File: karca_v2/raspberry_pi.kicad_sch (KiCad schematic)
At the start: 10 parts, among them J12 Conn_02x10_Odd_Even, Q2 PN2222A, U13 M41T93

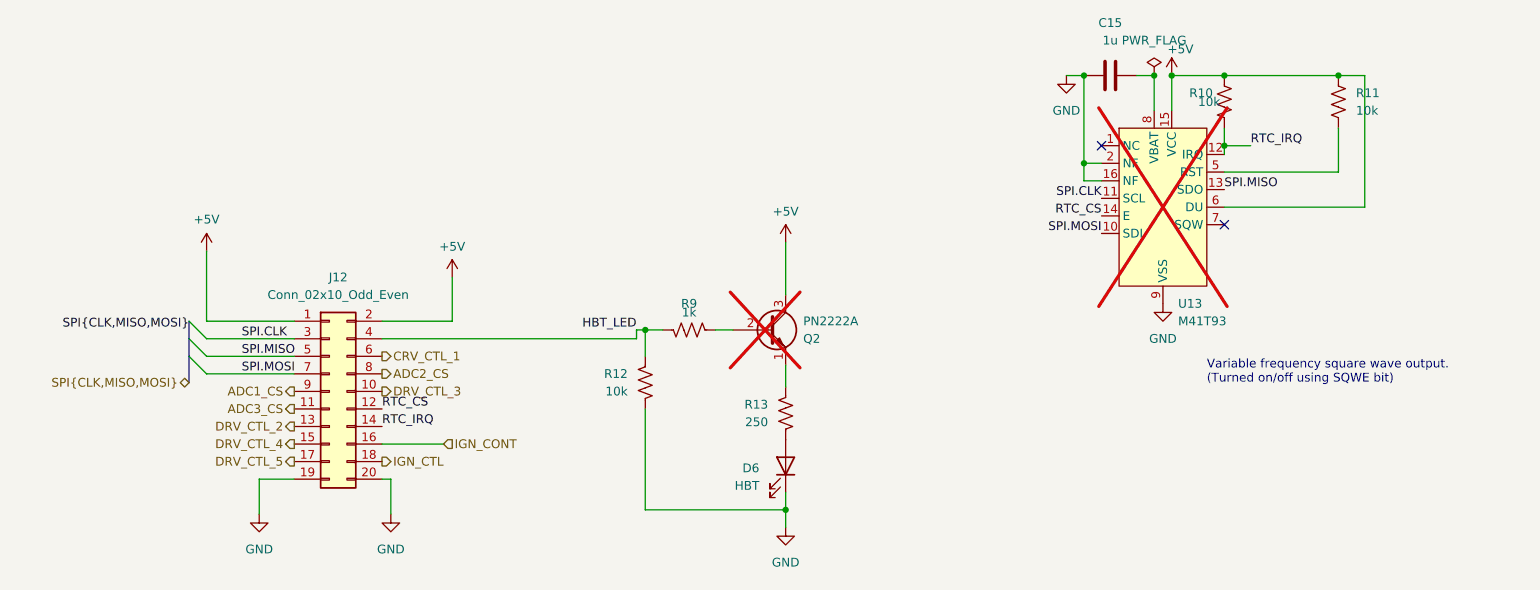
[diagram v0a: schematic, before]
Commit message: reorganized ADCs
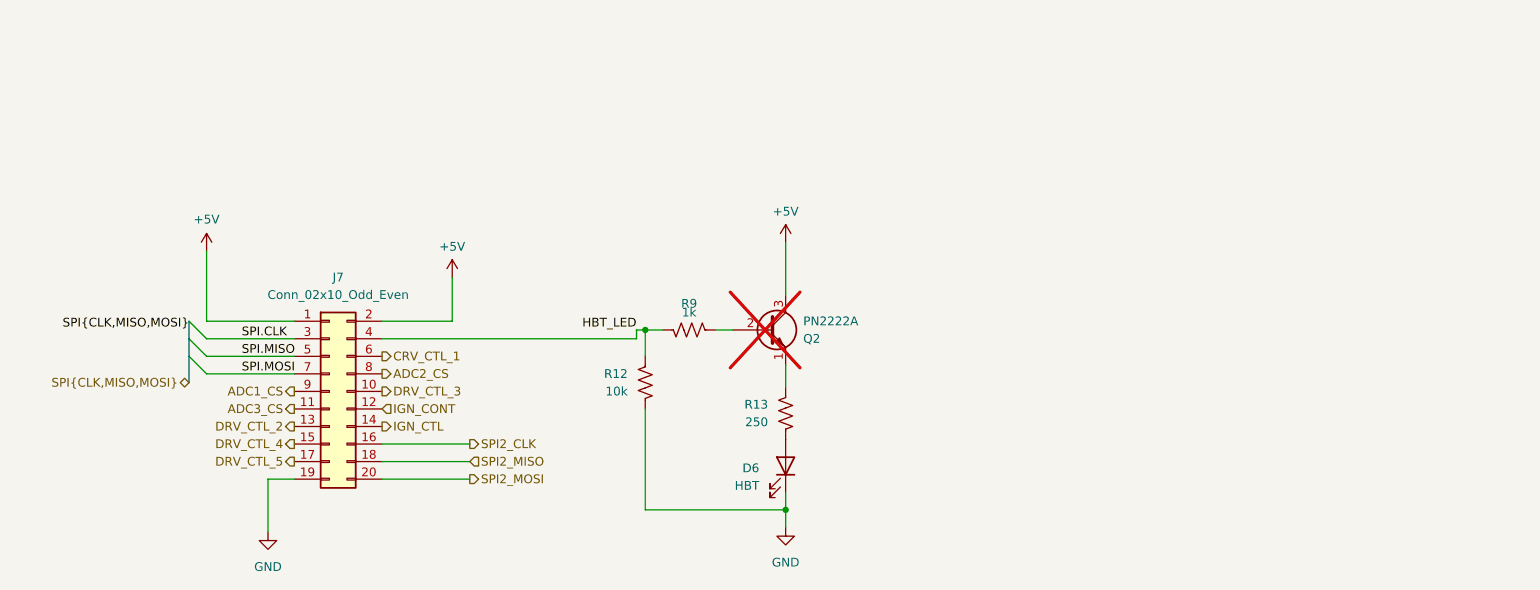
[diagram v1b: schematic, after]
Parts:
- removed C15: 1u, Capacitor_SMD:C_1206_3216Metric, symbol Device:C
- removed J12: Conn_02x10_Odd_Even, Connector_PinSocket_2.54mm:PinSocket_2x10_P2.54mm_Vertical, symbol Connector_Generic:Conn_02x10_Odd_Even
- removed R10, R11: 10k, Resistor_SMD:R_1206_3216Metric, symbol Device:R_US
- removed U13: M41T93, Package_SO:SOIC-18W_7.5x11.6mm_P1.27mm, symbol karca_lib:M41T93
- added J7: Conn_02x10_Odd_Even, symbol Connector_Generic:Conn_02x10_Odd_Even
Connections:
- net +5V: now also J7.1 (Pin_1), J7.2 (Pin_2)
- net ADC1_CS: now also J7.9 (Pin_9)
- net ADC2_CS: now also J7.8 (Pin_8)
- net ADC3_CS: now also J7.11 (Pin_11)
- net CRV_CTL_1: now also J7.6 (Pin_6)
- net DRV_CTL_2: now also J7.13 (Pin_13)
- net DRV_CTL_3: now also J7.10 (Pin_10)
- net DRV_CTL_4: now also J7.15 (Pin_15)
- net DRV_CTL_5: now also J7.17 (Pin_17)
- net GND: now also J7.19 (Pin_19)
- net HBT_LED: now also J7.4 (Pin_4)
- net IGN_CONT: now also J7.12 (Pin_12)
- net IGN_CTL: now also J7.14 (Pin_14)
- net SPI.CLK: now also J7.3 (Pin_3)
- net SPI.MISO: now also J7.5 (Pin_5)
- net SPI.MOSI: now also J7.7 (Pin_7)
- new net SPI2_CLK: J7.16 (Pin_16)
- new net SPI2_MISO: J7.18 (Pin_18)
- new net SPI2_MOSI: J7.20 (Pin_20)
- no-connect marks 2 -> 0
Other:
- note removed: "Variable frequency square wave output. (Turned on/off using SQWE bit)"

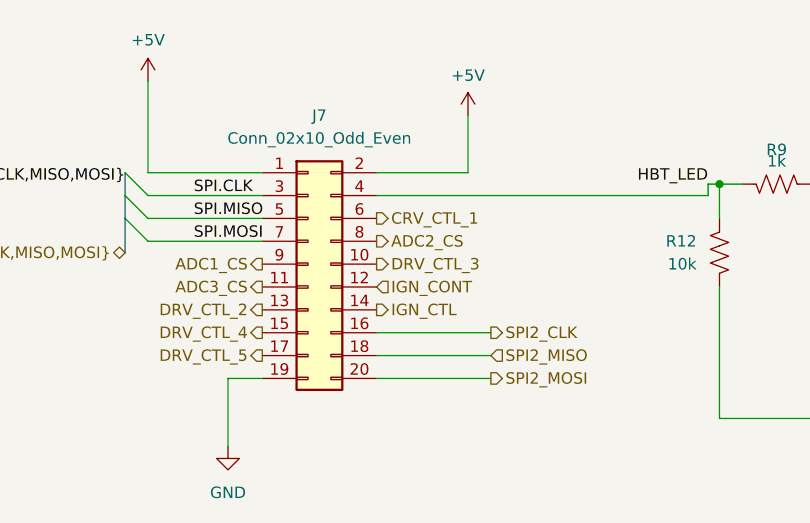
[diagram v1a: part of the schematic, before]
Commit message: swapped adcs
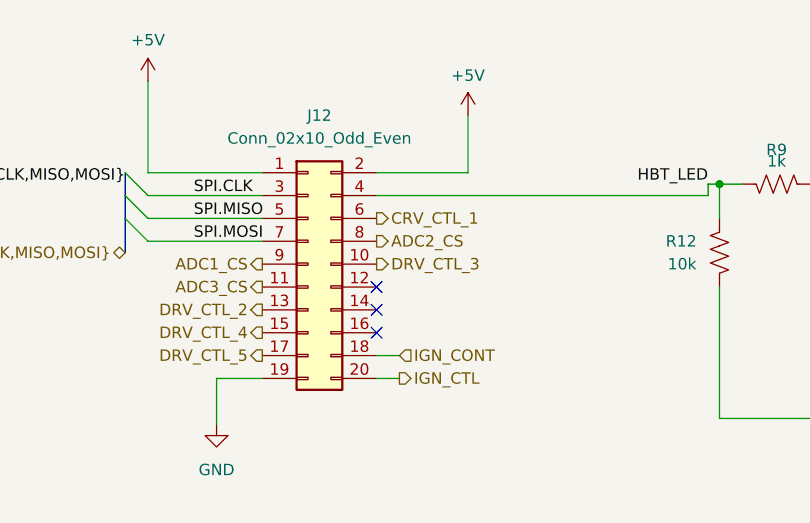
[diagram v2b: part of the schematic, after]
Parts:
- removed J7: Conn_02x10_Odd_Even, symbol Connector_Generic:Conn_02x10_Odd_Even
- added J12: Conn_02x10_Odd_Even, Connector_PinSocket_2.54mm:PinSocket_2x10_P2.54mm_Vertical, symbol Connector_Generic:Conn_02x10_Odd_Even
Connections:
- net +5V: now also J12.1 (Pin_1), J12.2 (Pin_2)
- net ADC1_CS: now also J12.9 (Pin_9)
- net ADC2_CS: now also J12.8 (Pin_8)
- net ADC3_CS: now also J12.11 (Pin_11)
- net CRV_CTL_1: now also J12.6 (Pin_6)
- net DRV_CTL_2: now also J12.13 (Pin_13)
- net DRV_CTL_3: now also J12.10 (Pin_10)
- net DRV_CTL_4: now also J12.15 (Pin_15)
- net DRV_CTL_5: now also J12.17 (Pin_17)
- net GND: now also J12.19 (Pin_19)
- net HBT_LED: now also J12.4 (Pin_4)
- net IGN_CONT: now also J12.18 (Pin_18)
- net IGN_CTL: now also J12.20 (Pin_20)
- net SPI.CLK: now also J12.3 (Pin_3)
- net SPI.MISO: now also J12.5 (Pin_5)
- net SPI.MOSI: now also J12.7 (Pin_7)
- no-connect marks 0 -> 3
